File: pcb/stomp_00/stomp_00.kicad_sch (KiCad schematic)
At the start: 4 parts, among them U1 Teensy4.1, U2 74HC595, U5 74HC165, U7 74HC4051

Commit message: came back to the project
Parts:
- removed U1: Teensy4.1, symbol teensy:Teensy4.1
- added H1, H2, H3, H4: MountingHole, MountingHole:MountingHole_3.2mm_M3, symbol Mechanical:MountingHole
- added J5, J6, J7: Conn_01x08_Pin, Connector_PinHeader_2.54mm:PinHeader_1x08_P2.54mm_Vertical, symbol Connector:Conn_01x08_Pin
- added U10: Teensy4.0, symbol teensy:Teensy4.0
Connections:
- net +5V: now also U10.52 (39_DAT2_TX5)
- net DAC_BCLK: now also U10.28 (21_A7_RX5_BCLK1)
- net DAC_DIN: now also U10.11 (9_OUT1C)
- net DAC_DOUT: now also U10.12 (10_CS_MQSR)
- net DAC_LRCLK: now also U10.27 (20_A6_TX5_LRCLK1)
- net DAC_MCLK: now also U10.30 (23_A9_CRX1_MCLK1)
- net DAC_SCL: now also U10.26 (19_A5_SCL0)
- net DAC_SDA: now also U10.25 (18_A4_SDA0)

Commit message: more sheets
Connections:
- net MIDI_IN: now reaches U10.2 (0_RX1_CRX2_CS1)
- net MIDI_OUT: now reaches U10.3 (1_TX1_CTX2_MISO1)
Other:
- added sheet Analog inputs (analoginput.kicad_sch)
- added sheet Digital inputs (digitalinput.kicad_sch)
- added sheet Digital outputs (digitaloutput.kicad_sch)
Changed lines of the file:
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@@
+    )
+  )
+  (global_label "MIDI_IN" (shape input) (at 121.92 49.53 180) (fields_autoplaced)
+    (effects (font (size 1.27 1.27)) (justify right))
+    (property "Intersheetrefs" "${INTERSHEET_REFS}" (at 112.1803 49.53 0)
+      (effects (font (size 1.27 1.27)) (justify right) hide)
     )
   )
@@
     (effects (font (size 1.27 1.27)) (justify right))
     (property "Intersheetrefs" "${INTERSHEET_REFS}" (at 110.9104 110.49 0)
+      (effects (font (size 1.27 1.27)) (justify right) hide)
+    )
+  )
+  (global_label "MIDI_OUT" (shape output) (at 121.92 52.07 180) (fields_autoplaced)
+    (effects (font (size 1.27 1.27)) (justify right))
+    (property "Intersheetrefs" "${INTERSHEET_REFS}" (at 110.487 52.07 0)
       (effects (font (size 1.27 1.27)) (justify right) hide)
     )
@@
     )
   )
+  (sheet (at 20.32 101.6) (size 12.7 5.207) (fields_autoplaced)
+    (stroke (width 0.1524) (type solid))
+    (fill (color 0 0 0 0.0000))
+    (property "Sheetname" "Digital outputs" (at 20.32 100.8884 0)
+      (effects (font (size 1.27 1.27)) (justify left bottom))
+    )
+    (property "Sheetfile" "digitaloutput.kicad_sch" (at 20.32 107.3916 0)
+      (effects (font (size 1.27 1.27)) (justify left top))
+    )
+    (instances
+      (project "stomp_00"
+        (path "/8f4a2eb0-078b-46cb-b534-a4acd11d130e" (page "8"))
+      )
+    )
+  )
   (sheet (at 20.32 22.733) (size 12.7 5.207) (fields_autoplaced)
     (stroke (width 0.1524) (type solid))
@@
       )
     )
+  )
+  (sheet (at 20.32 87.63) (size 12.7 5.207) (fields_autoplaced)
+    (stroke (width 0.1524) (type solid))
+    (fill (color 0 0 0 0.0000))
+    (property "Sheetname" "Digital inputs" (at 20.32 86.9184 0)
+      (effects (font (size 1.27 1.27)) (justify left bottom))
+    )
+    (property "Sheetfile" "digitalinput.kicad_sch" (at 20.32 93.4216 0)
+      (effects (font (size 1.27 1.27)) (justify left top))
+    )
+    (instances
+      (project "stomp_00"
+        (path "/8f4a2eb0-078b-46cb-b534-a4acd11d130e" (page "7"))
+      )
+    )
+  )
+  (sheet (at 20.32 73.66) (size 12.7 5.207) (fields_autoplaced)
+    (stroke (width 0.1524) (type solid))
+    (fill (color 0 0 0 0.0000))
+    (property "Sheetname" "Analog inputs" (at 20.32 72.9484 0)
+      (effects (font (size 1.27 1.27)) (justify left bottom))
+    )
+    (property "Sheetfile" "analoginput.kicad_sch" (at 20.32 79.4516 0)
+      (effects (font (size 1.27 1.27)) (justify left top))
+    )
+    (instances
+      (project "stomp_00"
+        (path "/8f4a2eb0-078b-46cb-b534-a4acd11d130e" (page "6"))
+      )
+    )

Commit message: adding all the components...
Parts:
- removed U2: 74HC595, Package_SO:SOIC-16_3.9x9.9mm_P1.27mm, symbol 74xx:74HC595
- removed U5: 74HC165, Package_SO:SOIC-16_3.9x9.9mm_P1.27mm, symbol 74xx:74HC165
- removed U7: 74HC4051, Package_SO:SOIC-16_3.9x9.9mm_P1.27mm, symbol 74xx:74HC4051
- added J6: Micro_SD_Card, misc:YAMAICHI_MICROSD_VERTICAL, symbol Connector:Micro_SD_Card
- added J9: Conn_01x04_Pin, symbol Connector:Conn_01x04_Pin
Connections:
- new net +3.3V: J6.4 (VDD)
- new net GND: J6.6 (VSS), J6.9 (SHIELD)
- new net SD_CHIP_SELECT: J6.2 (DAT3/CD)
- new net SD_CLOCK: J6.5 (CLK)
- new net SD_SERIAL_IN: J6.3 (CMD)
- new net SD_SERIAL_OUT: J6.7 (DAT0)
- no-connect marks 0 -> 2
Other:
- added sheet MIDI (midi.kicad_sch)

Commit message: not much
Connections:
- net +5V: no longer U10.52 (39_DAT2_TX5)
- net 165_CLOCK: now also U10.8 (6_OUT1D)
- net 165_DATA: now also U10.11 (9_OUT1C)
- net 165_LOAD: now also U10.7 (5_IN2)
- net 4051_ADDRESS_A: now also U10.23 (16_A2_RX4_SCL1)
- net 4051_ADDRESS_B: now also U10.24 (17_A3_TX4_SDA1)
- net 4051_ADDRESS_C: now also U10.29 (22_A8_CTX1)
- net 4051_READING_0: now also U10.21 (14_A0_TX3_SPDIF_OUT)
- net 4051_READING_1: now also U10.22 (15_A1_RX3_SPDIF_IN)
- net 595_CLOCK: now also U10.5 (3_LRCLK2)
- net 595_DATA: now also U10.4 (2_OUT2)
- net 595_LATCH: now also U10.6 (4_BCLK2)
- net DAC_DIN: now also U10.9 (7_RX2_OUT1A); no longer U10.11 (9_OUT1C)
- net DAC_DOUT: now also U10.10 (8_TX2_IN1); no longer U10.12 (10_CS_MQSR)
- net SD_CHIP_SELECT: now also U10.12 (10_CS_MQSR)
- net SD_CLOCK: now also U10.20 (13_SCK_CRX1_LED)
- net SD_SERIAL_IN: now also U10.13 (11_MOSI_CTX1)
- net SD_SERIAL_OUT: now also U10.14 (12_MISO_MQSL)

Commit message: taking shape...
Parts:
- removed J6: Micro_SD_Card, misc:YAMAICHI_MICROSD_VERTICAL, symbol Connector:Micro_SD_Card
- removed U10: Teensy4.0, symbol teensy:Teensy4.0
- added U7: Teensy4.1, symbol teensy:Teensy4.1
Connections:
- no-connect marks 2 -> 0

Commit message: teensy footprint
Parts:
- U7: footprint (none) -> teensy:Teensy41
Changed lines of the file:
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@@
     )
   )
-  (symbol (lib_id "Connector:Conn_01x08_Pin") (at 223.52 118.11 0) (unit 1)
-    (in_bom yes) (on_board yes) (dnp no) (fields_autoplaced)
-    (property "Reference" "J7" (at 224.155 107.4039 0)
-      (effects (font (size 1.27 1.27)))
-    )
-    (property "Value" "Conn_01x08_Pin" (at 224.155 109.3249 0)
-      (effects (font (size 1.27 1.27)))
-    )
-    (property "Footprint" "Connector_PinHeader_2.54mm:PinHeader_1x08_P2.54mm_Vertical" (at 223.52 118.11 0)
-      (effects (font (size 1.27 1.27)) hide)
-    )
-    (property "Datasheet" "~" (at 223.52 118.11 0)
-      (effects (font (size 1.27 1.27)) hide)
-    )
-    (pin "1")
-    (pin "2")
-    (pin "3")
-    (pin "4")
-    (pin "5")
-    (pin "6")
-    (pin "7")
-    (pin "8")
-    (instances
-      (project "stomp_00"
-        (path "/8f4a2eb0-078b-46cb-b534-a4acd11d130e"
-          (reference "J7") (unit 1)
-        )
-      )
-    )
-  )
-  (symbol (lib_id "Connector:Conn_01x04_Pin") (at 129.54 160.02 0) (unit 1)
-    (in_bom yes) (on_board yes) (dnp no) (fields_autoplaced)
-    (property "Reference" "J9" (at 130.175 153.67 0)
-      (effects (font (size 1.27 1.27)))
-    )
-    (property "Value" "Conn_01x04_Pin" (at 130.175 156.21 0)
-      (effects (font (size 1.27 1.27)))
-    )
-    (property "Footprint" "" (at 129.54 160.02 0)
-      (effects (font (size 1.27 1.27)) hide)
-    )
-    (property "Datasheet" "~" (at 129.54 160.02 0)
-      (effects (font (size 1.27 1.27)) hide)
-    )
-    (pin "1")
-    (pin "2")
-    (pin "3")
-    (pin "4")
-    (instances
-      (project "stomp_00"
-        (path "/8f4a2eb0-078b-46cb-b534-a4acd11d130e"
-          (reference "J9") (unit 1)
-        )
-      )
-    )
-  )
-  (symbol (lib_id "Mechanical:MountingHole") (at 214.63 30.48 0) (unit 1)
-    (in_bom yes) (on_board yes) (dnp no) (fields_autoplaced)
-    (property "Reference" "H2" (at 217.17 29.8363 0)
-      (effects (font (size 1.27 1.27)) (justify left))
-    )
-    (property "Value" "MountingHole" (at 217.17 31.7573 0)
-      (effects (font (size 1.27 1.27)) (justify left))
-    )
-    (property "Footprint" "MountingHole:MountingHole_3.2mm_M3" (at 214.63 30.48 0)
-      (effects (font (size 1.27 1.27)) hide)
-    )
-    (property "Datasheet" "~" (at 214.63 30.48 0)
-      (effects (font (size 1.27 1.27)) hide)
-    )
-    (instances
-      (project "stomp_00"
-        (path "/8f4a2eb0-078b-46cb-b534-a4acd11d130e"
-          (reference "H2") (unit 1)
-        )
-      )
-    )
-  )
-  (symbol (lib_id "Mechanical:MountingHole") (at 214.63 40.64 0) (unit 1)
-    (in_bom yes) (on_board yes) (dnp no) (fields_autoplaced)
-    (property "Reference" "H4" (at 217.17 39.9963 0)
-      (effects (font (size 1.27 1.27)) (justify left))
-    )
-    (property "Value" "MountingHole" (at 217.17 41.9173 0)
-      (effects (font (size 1.27 1.27)) (justify left))
-    )
-    (property "Footprint" "MountingHole:MountingHole_3.2mm_M3" (at 214.63 40.64 0)
-      (effects (font (size 1.27 1.27)) hide)
-    )
-    (property "Datasheet" "~" (at 214.63 40.64 0)
-      (effects (font (size 1.27 1.27)) hide)
-    )
-    (instances
-      (project "stomp_00"
-        (path "/8f4a2eb0-078b-46cb-b534-a4acd11d130e"
-          (reference "H4") (unit 1)
-        )
-      )
-    )
-  )
-  (symbol (lib_id "Mechanical:MountingHole") (at 214.63 25.4 0) (unit 1)
-    (in_bom yes) (on_board yes) (dnp no) (fields_autoplaced)
-    (property "Reference" "H1" (at 217.17 24.7563 0)
-      (effects (font (size 1.27 1.27)) (justify left))
-    )
-    (property "Value" "MountingHole" (at 217.17 26.6773 0)
-      (effects (font (size 1.27 1.27)) (justify left))
-    )
-    (property "Footprint" "MountingHole:MountingHole_3.2mm_M3" (at 214.63 25.4 0)
-      (effects (font (size 1.27 1.27)) hide)
-    )
-    (property "Datasheet" "~" (at 214.63 25.4 0)
-      (effects (font (size 1.27 1.27)) hide)
-    )
-    (instances
-      (project "stomp_00"
-        (path "/8f4a2eb0-078b-46cb-b534-a4acd11d130e"
-          (reference "H1") (unit 1)
-        )
-      )
-    )
-  )
-  (symbol (lib_id "teensy:Teensy4.1") (at 153.67 96.52 0) (unit 1)
-    (in_bom yes) (on_board yes) (dnp no) (fields_autoplaced)
-    (property "Reference" "U7" (at 153.67 32.6771 0)
-      (effects (font (size 1.27 1.27)))
-    )
-    (property "Value" "Teensy4.1" (at 153.67 34.5981 0)
-      (effects (font (size 1.27 1.27)))
-    )
-    (property "Footprint" "" (at 143.51 86.36 0)
-      (effects (font (size 1.27 1.27)) hide)
-    )
-    (property "Datasheet" "" (at 143.51 86.36 0)
+  (symbol (lib_id "teensy:Teensy4.1") (at 160.02 95.25 0) (unit 1)
+    (in_bom yes) (on_board yes) (dnp no) (fields_autoplaced)
+    (property "Reference" "U7" (at 160.02 31.4071 0)
+      (effects (font (size 1.27 1.27)))
+    )
+    (property "Value" "Teensy4.1" (at 160.02 33.3281 0)
+      (effects (font (size 1.27 1.27)))
+    )
+    (property "Footprint" "teensy:Teensy41" (at 149.86 85.09 0)
+      (effects (font (size 1.27 1.27)) hide)
+    )
+    (property "Datasheet" "" (at 149.86 85.09 0)
       (effects (font (size 1.27 1.27)) hide)
     )
@@
         )
       )
+    )
+  )
+  (symbol (lib_id "Connector:Conn_01x08_Pin") (at 223.52 118.11 0) (unit 1)
+    (in_bom yes) (on_board yes) (dnp no) (fields_autoplaced)
+    (property "Reference" "J7" (at 224.155 107.4039 0)
+      (effects (font (size 1.27 1.27)))
+    )
+    (property "Value" "Conn_01x08_Pin" (at 224.155 109.3249 0)
+      (effects (font (size 1.27 1.27)))
+    )
+    (property "Footprint" "Connector_PinHeader_2.54mm:PinHeader_1x08_P2.54mm_Vertical" (at 223.52 118.11 0)
+      (effects (font (size 1.27 1.27)) hide)
+    )
+    (property "Datasheet" "~" (at 223.52 118.11 0)
+      (effects (font (size 1.27 1.27)) hide)
+    )
+    (pin "1")
+    (pin "2")
+    (pin "3")
+    (pin "4")
+    (pin "5")
+    (pin "6")
+    (pin "7")
+    (pin "8")
+    (instances
+      (project "stomp_00"
+        (path "/8f4a2eb0-078b-46cb-b534-a4acd11d130e"
+          (reference "J7") (unit 1)
+        )
+      )
+    )
+  )
+  (symbol (lib_id "Connector:Conn_01x04_Pin") (at 129.54 160.02 0) (unit 1)
+    (in_bom yes) (on_board yes) (dnp no) (fields_autoplaced)
+    (property "Reference" "J9" (at 130.175 153.67 0)
+      (effects (font (size 1.27 1.27)))
+    )
+    (property "Value" "Conn_01x04_Pin" (at 130.175 156.21 0)
+      (effects (font (size 1.27 1.27)))
+    )
+    (property "Footprint" "" (at 129.54 160.02 0)
+      (effects (font (size 1.27 1.27)) hide)
+    )
+    (property "Datasheet" "~" (at 129.54 160.02 0)
+      (effects (font (size 1.27 1.27)) hide)
+    )
+    (pin "1")
+    (pin "2")
+    (pin "3")
+    (pin "4")
+    (instances
+      (project "stomp_00"
+        (path "/8f4a2eb0-078b-46cb-b534-a4acd11d130e"
+          (reference "J9") (unit 1)
+        )
+      )
+    )
+  )
+  (symbol (lib_id "Mechanical:MountingHole") (at 214.63 30.48 0) (unit 1)
+    (in_bom yes) (on_board yes) (dnp no) (fields_autoplaced)
+    (property "Reference" "H2" (at 217.17 29.8363 0)
+      (effects (font (size 1.27 1.27)) (justify left))
+    )
+    (property "Value" "MountingHole" (at 217.17 31.7573 0)
+      (effects (font (size 1.27 1.27)) (justify left))
+    )
+    (property "Footprint" "MountingHole:MountingHole_3.2mm_M3" (at 214.63 30.48 0)
+      (effects (font (size 1.27 1.27)) hide)
+    )
+    (property "Datasheet" "~" (at 214.63 30.48 0)
+      (effects (font (size 1.27 1.27)) hide)
+    )
+    (instances
+      (project "stomp_00"
+        (path "/8f4a2eb0-078b-46cb-b534-a4acd11d130e"
+          (reference "H2") (unit 1)
+        )
+      )
+    )
+  )
+  (symbol (lib_id "Mechanical:MountingHole") (at 214.63 40.64 0) (unit 1)
+    (in_bom yes) (on_board yes) (dnp no) (fields_autoplaced)
+    (property "Reference" "H4" (at 217.17 39.9963 0)
+      (effects (font (size 1.27 1.27)) (justify left))
+    )
+    (property "Value" "MountingHole" (at 217.17 41.9173 0)
+      (effects (font (size 1.27 1.27)) (justify left))
+    )
+    (property "Footprint" "MountingHole:MountingHole_3.2mm_M3" (at 214.63 40.64 0)
+      (effects (font (size 1.27 1.27)) hide)
+    )
+    (property "Datasheet" "~" (at 214.63 40.64 0)
+      (effects (font (size 1.27 1.27)) hide)
+    )
+    (instances
+      (project "stomp_00"
+        (path "/8f4a2eb0-078b-46cb-b534-a4acd11d130e"
+          (reference "H4") (unit 1)
+        )
+      )
+    )
+  )
+  (symbol (lib_id "Mechanical:MountingHole") (at 214.63 25.4 0) (unit 1)
+    (in_bom yes) (on_board yes) (dnp no) (fields_autoplaced)
+    (property "Reference" "H1" (at 217.17 24.7563 0)
+      (effects (font (size 1.27 1.27)) (justify left))
+    )
+    (property "Value" "MountingHole" (at 217.17 26.6773 0)
+      (effects (font (size 1.27 1.27)) (justify left))
+    )
+    (property "Footprint" "MountingHole:MountingHole_3.2mm_M3" (at 214.63 25.4 0)
+      (effects (font (size 1.27 1.27)) hide)
+    )
+    (property "Datasheet" "~" (at 214.63 25.4 0)
+      (effects (font (size 1.27 1.27)) hide)
+    )
+    (instances
+      (project "stomp_00"
+        (path "/8f4a2eb0-078b-46cb-b534-a4acd11d130e"
+          (reference "H1") (unit 1)
+        )
+      )

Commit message: seeing whether everything will fit...
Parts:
- removed J5, J6, J7: Conn_01x08_Pin, Connector_PinHeader_2.54mm:PinHeader_1x08_P2.54mm_Vertical, symbol Connector:Conn_01x08_Pin
- added J5, J6: Conn_01x24_Pin, Connector_PinHeader_2.54mm:PinHeader_1x24_P2.54mm_Vertical, symbol Connector:Conn_01x24_Pin
- added RV1, RV2, RV3: R_Potentiometer_US, Potentiometer_THT:Potentiometer_Piher_PC-16_Single_Vertical, symbol Device:R_Potentiometer_US
- added SW1: SW_DIP_x04, Button_Switch_THT:SW_DIP_SPSTx04_Slide_9.78x12.34mm_W7.62mm_P2.54mm, symbol Switch:SW_DIP_x04
- J9: footprint (none) -> Connector_PinHeader_2.54mm:PinHeader_1x04_P2.54mm_Vertical
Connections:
- net DAC_BCLK: now also U7.43 (21_A7_RX5_BCLK1)
- net DAC_DIN: now also U7.9 (7_RX2_OUT1A)
- net DAC_DOUT: now also U7.10 (8_TX2_IN1)
- net DAC_LRCLK: now also U7.42 (20_A6_TX5_LRCLK1)
- net DAC_MCLK: now also U7.45 (23_A9_CRX1_MCLK1)
- net DAC_SCL: now also U7.41 (19_A5_SCL)
- net DAC_SDA: now also U7.40 (18_A4_SDA)
- net MIDI_IN: now also U7.2 (0_RX1_CRX2_CS1)
- net MIDI_OUT: now also U7.3 (1_TX1_CTX2_MISO1)
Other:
- removed sheet Analog inputs
- removed sheet Digital inputs
- removed sheet Digital outputs

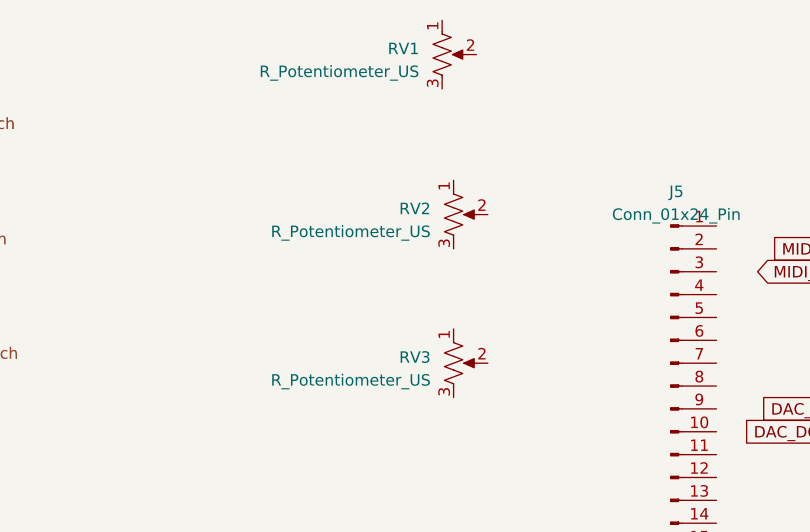
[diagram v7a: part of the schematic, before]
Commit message: input stage schematic
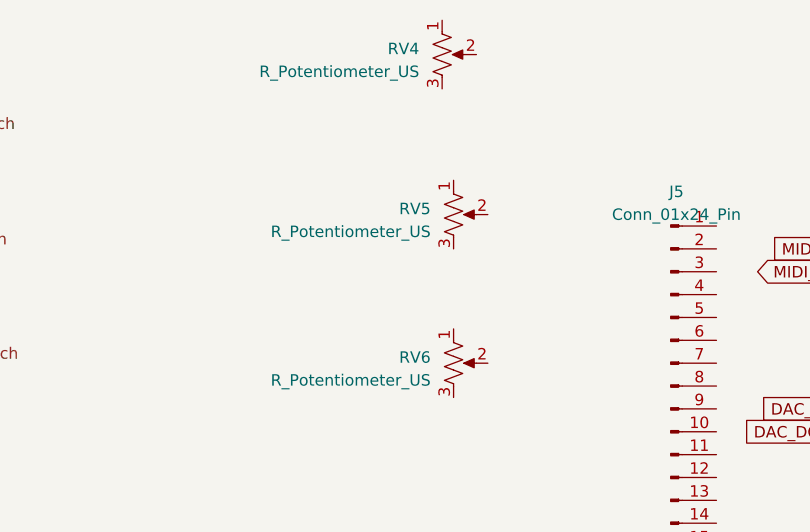
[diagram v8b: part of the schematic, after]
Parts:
- renumbered RV1 to RV4, RV2 to RV5, RV3 to RV6
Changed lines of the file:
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@@
   (symbol (lib_id "Device:R_Potentiometer_US") (at 86.36 21.59 0) (unit 1)
     (in_bom yes) (on_board yes) (dnp no) (fields_autoplaced)
-    (property "Reference" "RV1" (at 83.82 20.955 0)
+    (property "Reference" "RV4" (at 83.82 20.955 0)
       (effects (font (size 1.27 1.27)) (justify right))
     )
@@
   (symbol (lib_id "Device:R_Potentiometer_US") (at 87.63 39.37 0) (unit 1)
     (in_bom yes) (on_board yes) (dnp no) (fields_autoplaced)
-    (property "Reference" "RV2" (at 85.09 38.735 0)
+    (property "Reference" "RV5" (at 85.09 38.735 0)
       (effects (font (size 1.27 1.27)) (justify right))
     )
@@
   (symbol (lib_id "Device:R_Potentiometer_US") (at 87.63 55.88 0) (unit 1)
     (in_bom yes) (on_board yes) (dnp no) (fields_autoplaced)
-    (property "Reference" "RV3" (at 85.09 55.245 0)
+    (property "Reference" "RV6" (at 85.09 55.245 0)
       (effects (font (size 1.27 1.27)) (justify right))
     )
